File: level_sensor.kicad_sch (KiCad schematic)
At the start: 4 parts, among them J1 Conn_01x04_Socket, J2 Conn_01x04_Socket, J3 Screw_Terminal_01x04, U1 RS485_TTL_Sensor

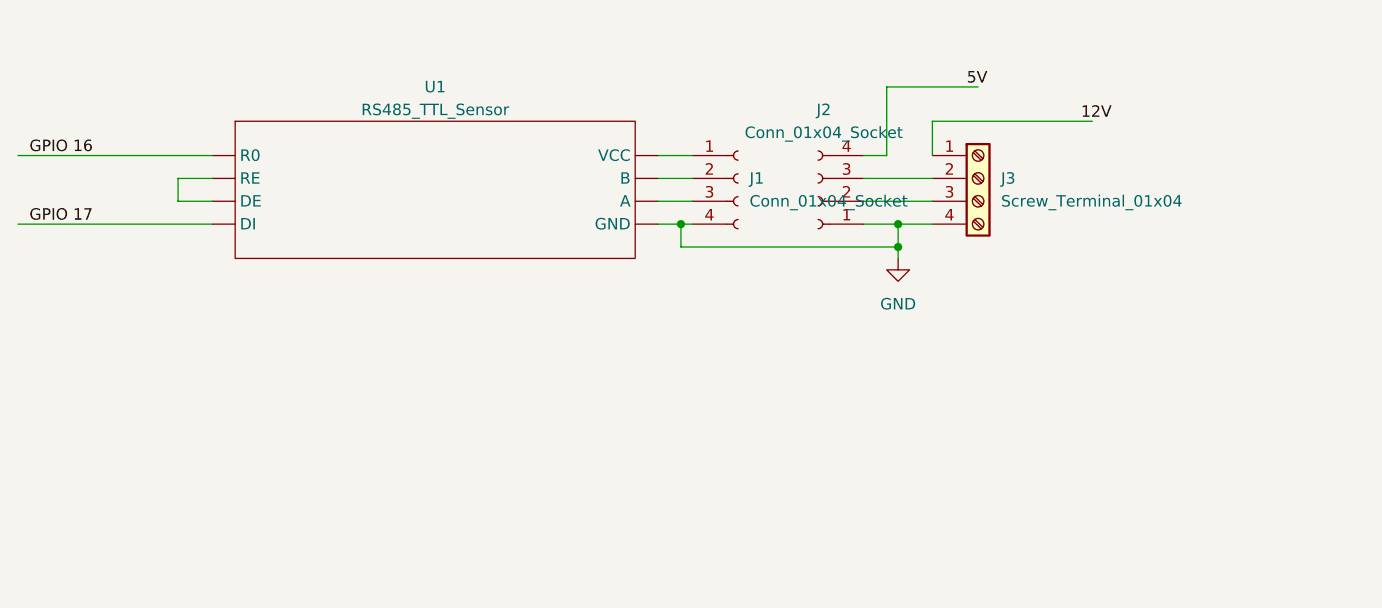
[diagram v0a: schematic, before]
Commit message: Pin label and notes
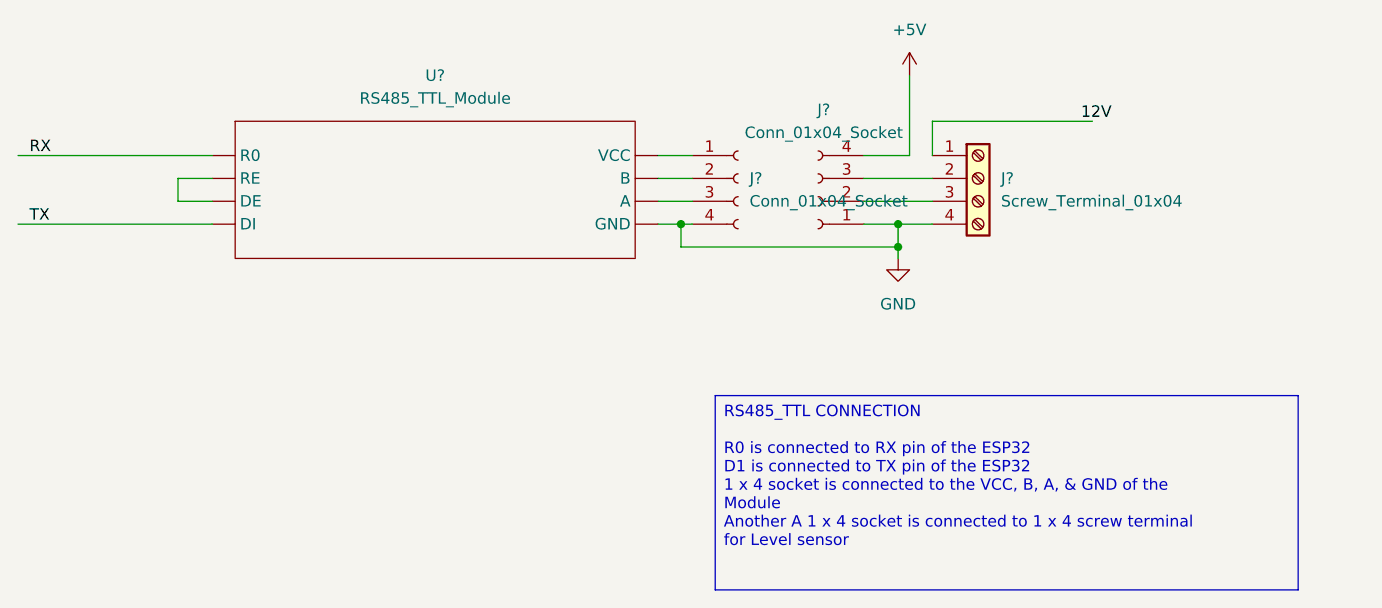
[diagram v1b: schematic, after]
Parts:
- U?: renamed from U1; value RS485_TTL_Sensor -> RS485_TTL_Module
- renumbered J3 to J?, J1 to J?, J2 to J?
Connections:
- net GPIO 16 is gone; now on net TX: U?. (GND)
- net GPIO 17 is gone; now on net TX: U?. (GND)
- net TX: now reaches U?. (GND)
- net 5V renamed +5V
- new net RX: U?. (GND)
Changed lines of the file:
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@@
 (kicad_sch
-	(version 20231120)
+	(version 20250114)
 	(generator "eeschema")
-	(generator_version "8.0")
+	(generator_version "9.0")
 	(paper "A4")
+	(text_box "RS485_TTL CONNECTION\n\nR0 is connected to RX pin of the ESP32\nD1 is connected to TX pin of the ESP32\n1 x 4 socket is connected to the VCC, B, A, & GND of the Module\nAnother A 1 x 4 socket is connected to 1 x 4 screw terminal for Level sensor "
+		(exclude_from_sim no)
+		(at 204.47 85.09 0)
+		(size 64.77 21.59)
+		(margins 0.9525 0.9525 0.9525 0.9525)
+		(stroke
+			(width 0)
+			(type solid)
+		)
+		(fill
+			(type none)
+		)
+		(effects
+			(font
+				(size 1.27 1.27)
+			)
+			(justify left top)
+		)
+	)
 	(junction
 		(at 200.66 66.04)
@@
 	(wire
 		(pts
-			(xy 220.98 58.42) (xy 223.52 58.42)
+			(xy 220.98 58.42) (xy 226.06 58.42)
 		)
 		(stroke
@@
 	(wire
 		(pts
-			(xy 223.52 50.8) (xy 233.68 50.8)
-		)
-		(stroke
-			(width 0)
-			(type default)
-		)
-	)
-	(wire
-		(pts
 			(xy 198.12 66.04) (xy 200.66 66.04)
 		)
@@
 	(wire
 		(pts
-			(xy 223.52 58.42) (xy 223.52 50.8)
+			(xy 226.06 58.42) (xy 226.06 49.53)
 		)
 		(stroke
@@
 	(label "12V"
 		(at 245.11 54.61 0)
-		(fields_autoplaced yes)
 		(effects
 			(font
@@
 		)
 	)
-	(label "5V"
-		(at 232.41 50.8 0)
-		(fields_autoplaced yes)
+	(label "RX"
+		(at 128.27 58.42 0)
 		(effects
 			(font
@@
 		)
 	)
-	(label "GPIO 16"
-		(at 128.27 58.42 0)
-		(fields_autoplaced yes)
-		(effects
-			(font
-				(size 1.27 1.27)
-			)
-			(justify left bottom)
-		)
-	)
-	(label "GPIO 17"
+	(label "TX"
 		(at 128.27 66.04 0)
-		(fields_autoplaced yes)
 		(effects
 			(font
@@
 		(dnp no)
 		(fields_autoplaced yes)
-		(property "Reference" "J3"
+		(property "Reference" "J?"
 			(at 236.22 60.9599 0)
 			(effects
@@
 		(pin "3"
 		)
-		(instances)
+		(instances
+			(project "fpc"
+				(path "/b29cf43f-9c9a-4a3e-a4af-0b82845645a8/683988a6-19dd-4cd0-af75-ddcf085acea1"
+					(reference "J?")
+					(unit 1)
+				)
+			)
+		)
 	)
 	(symbol
@@
 		(dnp no)
 		(fields_autoplaced yes)
-		(property "Reference" "#PWR01"
+		(property "Reference" "#PWR?"
 			(at 224.79 76.2 0)
 			(effects
@@
 		(pin "1"
 		)
-		(instances)
+		(instances
+			(project "fpc"
+				(path "/b29cf43f-9c9a-4a3e-a4af-0b82845645a8/683988a6-19dd-4cd0-af75-ddcf085acea1"
+					(reference "#PWR?")
+					(unit 1)
+				)
+			)
+		)
 	)
 	(symbol
@@
 		(dnp no)
 		(fields_autoplaced yes)
-		(property "Reference" "J1"
+		(property "Reference" "J?"
 			(at 208.28 60.9599 0)
 			(effects
@@
 		(pin "1"
 		)
-		(instances)
+		(instances
+			(project "fpc"
+				(path "/b29cf43f-9c9a-4a3e-a4af-0b82845645a8/683988a6-19dd-4cd0-af75-ddcf085acea1"
+					(reference "J?")
+					(unit 1)
+				)
+			)
+		)
+	)
+	(symbol
+		(lib_id "power:+5V")
+		(at 226.06 49.53 0)
+		(unit 1)
+		(exclude_from_sim no)
+		(in_bom yes)
+		(on_board yes)
+		(dnp no)
+		(fields_autoplaced yes)
+		(property "Reference" "#PWR01"
+			(at 226.06 53.34 0)
+			(effects
+				(font
+					(size 1.27 1.27)
+				)
+				(hide yes)
+			)
+		)
+		(property "Value" "+5V"
+			(at 226.06 44.45 0)
+			(effects
+				(font
+					(size 1.27 1.27)
+				)
+			)
+		)
+		(property "Footprint" ""
+			(at 226.06 49.53 0)
+			(effects
+				(font
+					(size 1.27 1.27)
+				)
+				(hide yes)
+			)
+		)
+		(property "Datasheet" ""
+			(at 226.06 49.53 0)
+			(effects
+				(font
+					(size 1.27 1.27)
+				)
+				(hide yes)
+			)
+		)
+		(property "Description" "Power symbol creates a global label with name \"+5V\""
+			(at 226.06 49.53 0)
+			(effects
+				(font
+					(size 1.27 1.27)
+				)
+				(hide yes)
+			)
+		)
+		(pin "1"
+		)
+		(instances
+			(project ""
+				(path "/b29cf43f-9c9a-4a3e-a4af-0b82845645a8/683988a6-19dd-4cd0-af75-ddcf085acea1"
+					(reference "#PWR01")
+					(unit 1)
+				)
+			)
+		)
 	)
 	(symbol
@@
 		(dnp no)
 		(fields_autoplaced yes)
-		(property "Reference" "U1"
-			(at 173.355 50.8 0)
-			(effects
-				(font
-					(size 1.27 1.27)
-				)
-			)
-		)
-		(property "Value" "RS485_TTL_Sensor"
-			(at 173.355 53.34 0)
+		(property "Reference" "U?"
+			(at 173.355 49.53 0)
+			(effects
+				(font
+					(size 1.27 1.27)
+				)
+			)
+		)
+		(property "Value" "RS485_TTL_Module"
+			(at 173.355 52.07 0)
 			(effects
 				(font
@@
 		(pin ""
 		)
-		(instances)
+		(instances
+			(project "fpc"
+				(path "/b29cf43f-9c9a-4a3e-a4af-0b82845645a8/683988a6-19dd-4cd0-af75-ddcf085acea1"
+					(reference "U?")
+					(unit 1)
+				)
+			)
+		)
 	)
 	(symbol
@@
 		(dnp no)
 		(fields_autoplaced yes)
-		(property "Reference" "J2"
+		(property "Reference" "J?"
 			(at 216.535 53.34 0)
 			(effects
@@
 		(pin "3"
 		)
-		(instances)
+		(instances
+			(project "fpc"
+				(path "/b29cf43f-9c9a-4a3e-a4af-0b82845645a8/683988a6-19dd-4cd0-af75-ddcf085acea1"
+					(reference "J?")
+					(unit 1)
+				)
+			)
+		)
 	)
 )
